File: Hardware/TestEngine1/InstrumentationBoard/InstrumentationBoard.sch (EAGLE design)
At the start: 109 parts, among them IC1 MAX31855, J1 1X2-3.5MM, Q1 MOSFET-NCHANNELBSS123LT1G, Q2 MOSFET-NCHANNELBSS123LT1G, Q3 MOSFET-NCHANNELBSS123LT1G, U1 BMP180

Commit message: work in progress in laying out and routing instrument board
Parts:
- removed C11: 0.33uF, SparkFun-Capacitors:CAP0805
- removed C12: 0.1uF, SparkFun-Capacitors:CAP0805
- removed D1: 1n4148, adafruit:DIODESOD-323F
- removed D2: 1N4148, adafruit:DIODESOD-323F
- removed JP20: (no value), SparkFun-Connectors:M03PTH
- removed JP21, JP22, JP23, JP24: M02PTH, SparkFun-Connectors:M02PTH
- removed R18: 10K, adafruit:R-US_R0805
- removed U$8: MC33269DTRK, RitLaunchInitiative:MC33269DTRK
- added JP133: (no value), SparkFun-Connectors:M05PTH
- added JP1777: M02PTH, SparkFun-Connectors:M02PTH
- added JP55: (no value), SparkFun-Connectors:M04PTH
- added R35: 10K, SparkFun-Resistors:RESISTOR0805-RES
- added U$10: BOOSTER_PACK_CONNECTED, RitLaunchInitiative:BOOSTER_PACK_CONNECTED
- C1, C2: device adafruit:C-USC0805K -> SparkFun-Capacitors:CAP0805
- JP11, JP14, JP15: value (none) -> M02PTH; device SparkFun-Connectors:M03PTH -> SparkFun-Connectors:M02PTH
- JP12, JP5: value (none) -> M02PTH; device SparkFun-Connectors:M04PTH -> SparkFun-Connectors:M02PTH
- JP13: value (none) -> M02PTH; device SparkFun-Connectors:M05PTH -> SparkFun-Connectors:M02PTH
- JP17, JP18, JP9: value M02PTH -> (none); device SparkFun-Connectors:M02PTH -> SparkFun-Connectors:M03PTH
- R1, R2, R8: value 10K -> 10k; device adafruit:R-US_R0805 -> SparkFun-Resistors:RESISTOR0805-RES
- R10, R11, R30, R34, R9: device adafruit:R-US_R0805 -> SparkFun-Resistors:RESISTOR0805-RES
- R12, R25: value 1.7k -> 10K
- R13, R26: value 3.3k -> 10K
- R14: value 68 -> 1.7k; device adafruit:R-US_R0805 -> SparkFun-Resistors:RESISTOR0805-RES
- R15: value 0 -> 3.3k; device adafruit:R-US_R0805 -> SparkFun-Resistors:RESISTOR0805-RES
- R16: value 0 -> 1.7k; device adafruit:R-US_R0805 -> SparkFun-Resistors:RESISTOR0805-RES
- R17: value 10K -> 3.3k; device adafruit:R-US_R0805 -> SparkFun-Resistors:RESISTOR0805-RES
- R19: value 10K -> 9k; device adafruit:R-US_R0805 -> SparkFun-Resistors:RESISTOR0805-RES
- R20: value 10K -> 3k; device adafruit:R-US_R0805 -> SparkFun-Resistors:RESISTOR0805-RES
- R21: value 10K -> 100; device adafruit:R-US_R0805 -> SparkFun-Resistors:RESISTOR0805-RES
- R22: value 9k -> 220; device adafruit:R-US_R0805 -> SparkFun-Resistors:RESISTOR0805-RES
- R23: value 3k -> 680; device adafruit:R-US_R0805 -> SparkFun-Resistors:RESISTOR0805-RES
- R24, R31, R32: value 10k -> 10K
- R27: value 100 -> 68; device adafruit:R-US_R0805 -> SparkFun-Resistors:RESISTOR0805-RES
- R28: value 220 -> 0; device adafruit:R-US_R0805 -> SparkFun-Resistors:RESISTOR0805-RES
- R29: value 680 -> 0; device adafruit:R-US_R0805 -> SparkFun-Resistors:RESISTOR0805-RES
- R33: value 10k -> 1K
- R7: value 1K -> 10k; device adafruit:R-US_R0805 -> SparkFun-Resistors:RESISTOR0805-RES
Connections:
- removed net SCLK: D1.C
- removed net THERMOCOUPLE_CS: D2.C
- new net KEYSWITCH_1: JP25.1, R31.1
- net +3V3: now also JP1777.2, JP5.2, JP6.2, JP7.2, JP8.2, R21.1, R28.1, R29.1, R34.1, R35.1, U$10.3.3V; no longer JP12.2, JP17.2, JP18.2, JP22.2, JP23.2, JP24.2, R1.1, R14.1, R15.1, R16.1, R2.1
- net 12V: now also JP11.2, JP12.2, JP13.2, JP133.5, JP14.2, JP15.2, R19.1, R23.1; no longer C11.1, JP12.4, JP13.5, JP21.2, JP6.2, JP7.2, JP8.2, JP9.2, R22.1, R29.1, U$8.IN
- net 5V: now also JP17.2, JP18.2, JP19.2, JP9.1, R22.1, U$10.5V; no longer C12.1, JP12.3, JP14.2, JP15.2, JP19.1, JP20.2, R28.1, U$8.OUT
- net BATTVOLTAGE: now also R19.2, R20.1, U$10.AIN19/PK3; no longer R22.2, R23.1
- net BLUE: now also R26.1; no longer R17.1
- net CS: now also R35.2; no longer D2.A, R2.2
- net FET1: now also R9.1, U$10.T0CCP1/PL5; no longer R8.1
- net FET2: now also R10.1, U$10.PL0; no longer R9.1
- net FET3: now also R11.1, U$10.PL1; no longer R10.1
- net FET4: now also R12.1, U$10.PL2; no longer R11.1
- net FET5: now also R13.1, U$10.PL3; no longer R30.1
- net GND: now also JP133.3, JP133.4, JP17.3, JP18.3, JP55.4, JP9.3, R1.1, R12.2, R13.2, R15.1, R17.1, R2.1, R24.2, R25.2, R26.2, R31.2, R32.2, R7.1, R8.1, U$10.GND; no longer JP11.1, JP12.1, JP13.3, JP13.4, JP14.3, JP15.3, JP20.3, JP5.4, R13.1, R17.2, R18.2, R19.2, R21.2, R23.2, R24.1, R26.1, R31.1, R32.1, R33.1, R34.2, R8.2
- net GREEN: now also R25.1; no longer R18.1
- net LOADCELL: now also U$10.AIN18/PK2
- net N$10: now also R28.2; no longer R15.2
- net N$11: now also JP55.1; no longer JP5.1
- net N$12: no longer C11.2, C12.2, U$8.GND
- net N$13: now also R33.2; no longer R7.2
- net N$14: now also R33.1; no longer R7.1
- net N$15: now also R29.2; no longer R16.2
- net N$16: now also JP55.2; no longer JP5.2
- net N$17: now also JP14.1; no longer JP9.1
- net N$18: now also JP11.1; no longer JP6.1
- net N$19: now also JP12.1; no longer JP7.1
- net N$2: now also JP9.2, R14.2; no longer JP10.2, R12.2
- net N$20: now also JP55.3; no longer JP5.3
- net N$21: now also JP10.2, R16.2; no longer JP19.2, R25.2
- net N$22: now also JP13.1; no longer JP8.1
- net N$23: now also R22.2; no longer R28.2
- net N$24: now also R21.2; no longer R27.2
- net N$25: now also R23.2; no longer R29.2
- net N$26: now also JP15.1; no longer JP21.1
- net N$9: now also R27.2; no longer R14.2
- net PSI_1: now also R14.1, R15.2, U$10.AIN16/PK0; no longer R12.1, R13.2
- net PSI_2: now also R16.1, R17.2, U$10.AIN17/PK1; no longer R25.1, R26.2
- net PWM_1: now also JP16.1, U$10.M0PWM1/PF1; no longer JP14.1
- net PWM_2: now also JP17.1, U$10.M0PWM2/PF2; no longer JP15.1
- net PWM_3: now also JP18.1, U$10.M0PWM3/PF3; no longer JP16.1
- net PWM_4: now also JP19.1, U$10.M0PWM4/PG0; no longer JP20.1
- net RED: now also R24.1; no longer R19.1
- net SCK: now also R34.2; no longer D1.A, R1.2
- net SCL: now also JP133.2, U$10.I2C0SCL/PB2; no longer JP11.2, JP13.2
- net SDA: now also JP133.1, U$10.I2C0SDA/PB3; no longer JP11.3, JP13.1
- net SW_1: now also R32.1; no longer R20.1
- net TILTSWITCH_1: now also JP1777.1, R30.1; no longer JP17.1, JP25.1, R21.1, R34.1
- net TR1: now also R1.2; no longer R3.2
- net TR2: now also R2.2; no longer R4.2
- net TR3: now also R3.2; no longer R5.2
- net TR4: now also R4.2; no longer R6.2
- net TR5: now also JP5.1, R5.2; no longer JP18.1, R24.2
- net TR6: now also JP6.1, R6.2, U$10.AIN13/PD2; no longer JP22.1, R31.2
- net TR7: now also JP7.1, R7.2, U$10.AIN10/PB4; no longer JP23.1, R32.2
- net TR8: now also JP8.1, R8.2, U$10.AIN11/PB5; no longer JP24.1, R33.2
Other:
- note removed: "I2c"
- note removed: "Optional for additional current sink"
- moved on the sheet: JP10, JP16, JP19, JP6, JP7, JP8, R1, R10, R11, R12, R13, R14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

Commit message: work in progress on pcb's
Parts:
- added JP20: (no value), SparkFun-Connectors:M03PTH
- added R18: 1.7k, SparkFun-Resistors:RESISTOR0805-RES
- added R36: 3.3k, SparkFun-Resistors:RESISTOR0805-RES
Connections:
- new net N$27: JP20.2, R18.2
- new net PSI_3: R18.1, R36.2, U$10.AIN18/PK2
- net 5V: now also JP20.1
- net BATTVOLTAGE: now also U$10.PA6; no longer U$10.AIN19/PK3
- net BLUE: now also U$10.M0PWM7/PK5
- net CS: now also U$10.PQ1
- net GND: now also JP20.3, R36.1
- net GREEN: now also U$10.M0PWM6/PK4
- net KEYSWITCH_1: now also U$10.PH1
- net LOADCELL: now also U$10.AIN19/PK3; no longer U$10.AIN18/PK2
- net MISO: now also U$10.SSI3RX/PQ3
- net RED: now also U$10.M0PWM5/PG1
- net SCK: now also U$10.SSI3CLK/PQ0
- net SW_1: now also U$10.PK6
- net TILTSWITCH_1: now also U$10.PH0
- net TR1: now also U$10.AIN3/PE0
- net TR2: now also U$10.AIN2/PE1
- net TR3: now also U$10.AIN1/PE2
- net TR4: now also U$10.AIN0/PE3
- net TR5: now also U$10.AIN4/PD7

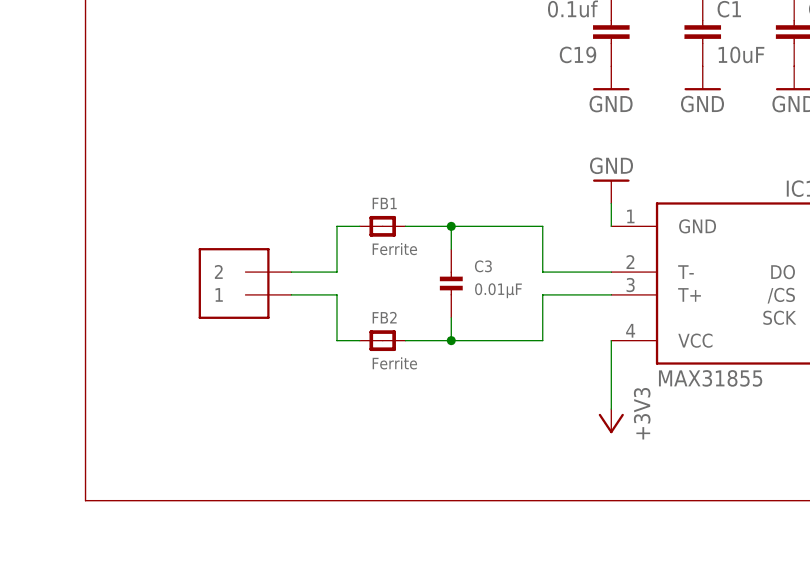
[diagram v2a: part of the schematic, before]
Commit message: power traces being layed out
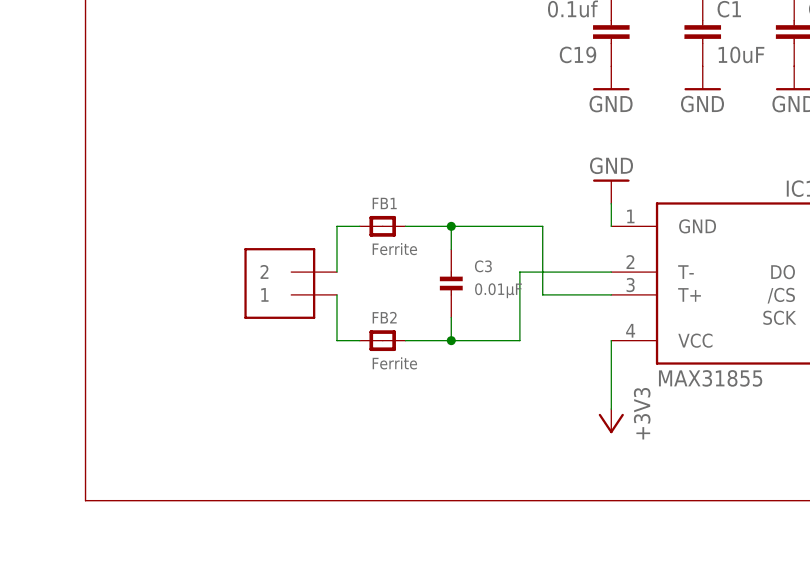
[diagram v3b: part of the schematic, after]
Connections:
- net N$4: now also IC1.T+; no longer IC1.T-
- net N$6: now also IC1.T-; no longer IC1.T+
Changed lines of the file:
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@@
 <instance part="IC1" gate="G$1" x="-88.9" y="134.62"/>
 <instance part="GND1" gate="1" x="-101.6" y="142.24" rot="R180"/>
-<instance part="J1" gate="G$1" x="-142.24" y="132.08" rot="R180"/>
+<instance part="J1" gate="G$1" x="-137.16" y="132.08" rot="R180"/>
 <instance part="+3V2" gate="G$1" x="-40.64" y="7.62"/>
 <instance part="+3V3" gate="G$1" x="-101.6" y="114.3" rot="R180"/>
@@
 <net name="N$1" class="0">
 <segment>
-<pinref part="J1" gate="G$1" pin="2"/>
-<wire x1="-137.16" y1="132.08" x2="-132.08" y2="132.08" width="0.1524" layer="91"/>
 <wire x1="-132.08" y1="132.08" x2="-132.08" y2="137.16" width="0.1524" layer="91"/>
 <pinref part="FB1" gate="G$1" pin="P$1"/>
 <wire x1="-132.08" y1="137.16" x2="-129.54" y2="137.16" width="0.1524" layer="91"/>
+<pinref part="J1" gate="G$1" pin="2"/>
 </segment>
 </net>
@@
 <wire x1="-119.38" y1="137.16" x2="-119.38" y2="134.62" width="0.1524" layer="91"/>
 <wire x1="-119.38" y1="137.16" x2="-109.22" y2="137.16" width="0.1524" layer="91"/>
-<wire x1="-109.22" y1="137.16" x2="-109.22" y2="132.08" width="0.1524" layer="91"/>
-<pinref part="IC1" gate="G$1" pin="T-"/>
-<wire x1="-109.22" y1="132.08" x2="-101.6" y2="132.08" width="0.1524" layer="91"/>
+<wire x1="-109.22" y1="137.16" x2="-109.22" y2="129.54" width="0.1524" layer="91"/>
 <junction x="-119.38" y="137.16"/>
+<pinref part="IC1" gate="G$1" pin="T+"/>
+<wire x1="-109.22" y1="129.54" x2="-101.6" y2="129.54" width="0.1524" layer="91"/>
 </segment>
 </net>
 <net name="N$5" class="0">
 <segment>
-<pinref part="J1" gate="G$1" pin="1"/>
-<wire x1="-137.16" y1="129.54" x2="-132.08" y2="129.54" width="0.1524" layer="91"/>
 <wire x1="-132.08" y1="129.54" x2="-132.08" y2="124.46" width="0.1524" layer="91"/>
 <pinref part="FB2" gate="G$1" pin="P$1"/>
 <wire x1="-132.08" y1="124.46" x2="-129.54" y2="124.46" width="0.1524" layer="91"/>
+<pinref part="J1" gate="G$1" pin="1"/>
 </segment>
 </net>
@@
 <wire x1="-124.46" y1="124.46" x2="-119.38" y2="124.46" width="0.1524" layer="91"/>
 <wire x1="-119.38" y1="124.46" x2="-119.38" y2="127" width="0.1524" layer="91"/>
-<wire x1="-119.38" y1="124.46" x2="-109.22" y2="124.46" width="0.1524" layer="91"/>
-<wire x1="-109.22" y1="124.46" x2="-109.22" y2="129.54" width="0.1524" layer="91"/>
+<wire x1="-119.38" y1="124.46" x2="-111.76" y2="124.46" width="0.1524" layer="91"/>
 <junction x="-119.38" y="124.46"/>
-<pinref part="IC1" gate="G$1" pin="T+"/>
-<wire x1="-109.22" y1="129.54" x2="-101.6" y2="129.54" width="0.1524" layer="91"/>
+<wire x1="-111.76" y1="124.46" x2="-111.76" y2="132.08" width="0.1524" layer="91"/>
+<pinref part="IC1" gate="G$1" pin="T-"/>
+<wire x1="-111.76" y1="132.08" x2="-101.6" y2="132.08" width="0.1524" layer="91"/>
 </segment>
 </net>

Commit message: majority of power and analog busses layed out
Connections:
- net BATTVOLTAGE: now also U$10.AIN19/PK3; no longer U$10.PA6
- net FET2: now also U$10.PL3; no longer U$10.PL0
- net FET3: now also U$10.PL0; no longer U$10.PL1
- net FET4: now also U$10.PL1; no longer U$10.PL2
- net FET5: now also U$10.PL2; no longer U$10.PL3
- net GND: now also JP10.2, JP20.2, JP9.2; no longer JP10.3, JP20.3, JP9.3
- net LOADCELL: now also U$10.AIN13/PD2; no longer U$10.AIN19/PK3
- net N$2: now also JP9.3; no longer JP9.2
- net N$21: now also JP10.3; no longer JP10.2
- net N$27: now also JP20.3; no longer JP20.2
- net PSI_1: now also U$10.AIN11/PB5; no longer U$10.AIN16/PK0
- net PSI_2: now also U$10.AIN16/PK0; no longer U$10.AIN17/PK1
- net PSI_3: now also U$10.AIN10/PB4; no longer U$10.AIN18/PK2
- net TR6: now also U$10.PA6; no longer U$10.AIN13/PD2
- net TR7: now also U$10.AIN17/PK1; no longer U$10.AIN10/PB4
- net TR8: now also U$10.AIN18/PK2; no longer U$10.AIN11/PB5
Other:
- moved on the sheet: JP10, JP9, R18

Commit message: work in progress
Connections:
- net GREEN: now also U$10.M0PWM5/PG1; no longer U$10.M0PWM6/PK4
- net RED: now also U$10.M0PWM6/PK4; no longer U$10.M0PWM5/PG1
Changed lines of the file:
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@@
 <segment>
 <wire x1="-50.8" y1="213.36" x2="-66.04" y2="213.36" width="0.1524" layer="91"/>
+<pinref part="U$10" gate="G$1" pin="M0PWM7/PK5"/>
 <label x="-50.8" y="213.36" size="1.016" layer="95" xref="yes"/>
-<pinref part="U$10" gate="G$1" pin="M0PWM7/PK5"/>
 </segment>
 </net>
@@
 </segment>
 <segment>
-<wire x1="-50.8" y1="215.9" x2="-66.04" y2="215.9" width="0.1524" layer="91"/>
-<label x="-50.8" y="215.9" size="1.016" layer="95" xref="yes"/>
-<pinref part="U$10" gate="G$1" pin="M0PWM6/PK4"/>
+<wire x1="-48.26" y1="218.44" x2="-66.04" y2="218.44" width="0.1524" layer="91"/>
+<label x="-48.26" y="218.44" size="1.016" layer="95" xref="yes"/>
+<pinref part="U$10" gate="G$1" pin="M0PWM5/PG1"/>
 </segment>
 </net>
@@
 </segment>
 <segment>
-<wire x1="-50.8" y1="218.44" x2="-66.04" y2="218.44" width="0.1524" layer="91"/>
-<label x="-50.8" y="218.44" size="1.016" layer="95" xref="yes"/>
-<pinref part="U$10" gate="G$1" pin="M0PWM5/PG1"/>
+<wire x1="-66.04" y1="215.9" x2="-55.88" y2="215.9" width="0.1524" layer="91"/>
+<label x="-55.88" y="215.9" size="1.016" layer="95" xref="yes"/>
+<pinref part="U$10" gate="G$1" pin="M0PWM6/PK4"/>
 </segment>
 </net>

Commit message: more work on board
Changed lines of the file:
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@@
 <wire x1="325.12" y1="220.98" x2="325.12" y2="289.56" width="0.1524" layer="94"/>
 <wire x1="325.12" y1="289.56" x2="190.5" y2="289.56" width="0.1524" layer="94"/>
-<text x="218.44" y="287.02" size="2.54" layer="94">Pressure transducers voltage signaling</text>
+<text x="226.06" y="284.48" size="2.54" layer="94">Pressure transducers voltage signaling</text>
 <wire x1="195.58" y1="106.68" x2="325.12" y2="106.68" width="0.1524" layer="94"/>
 <wire x1="325.12" y1="106.68" x2="325.12" y2="71.12" width="0.1524" layer="94"/>

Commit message: Finished bulk routing.
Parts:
- removed C16: 10uF, SparkFun-Capacitors:CAP0805
- removed C17: 0.1uf, SparkFun-Capacitors:CAP0805
- removed C18: 100pF, SparkFun-Capacitors:CAP0805
- added R37, R38: 10K, SparkFun-Resistors:RESISTOR0805-RES
- added S2: SWITCH-MOMENTARY-2SMD, SparkFun-Electromechanical:SWITCH-MOMENTARY-2SMD
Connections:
- new net RST: S2.1, U$10.RST
- net +3V3: now also R37.1, R38.1
- net 12V: no longer C16.1, C17.1, C18.1
- net GND: now also S2.2; no longer C16.2, C17.2, C18.2
- net SCL: now also R37.2
- net SDA: now also R38.2
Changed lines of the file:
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@@
 <part name="SUPPLY22" library="SparkFun-Aesthetics" deviceset="12V" device=""/>
 <part name="SUPPLY23" library="SparkFun-Aesthetics" deviceset="12V" device=""/>
-<part name="C16" library="SparkFun-Capacitors" deviceset="CAP" device="0805" value="10uF">
-<attribute name="DIGIKEY" value="490-3886-1-ND"/>
-</part>
-<part name="C17" library="SparkFun-Capacitors" deviceset="CAP" device="0805" value="0.1uf"/>
-<part name="C18" library="SparkFun-Capacitors" deviceset="CAP" device="0805" value="100pF"/>
 <part name="SUPPLY24" library="SparkFun-Aesthetics" deviceset="12V" device=""/>
 <part name="GND47" library="supply1" deviceset="GND" device=""/>
@@
 <part name="R36" library="SparkFun-Resistors" deviceset="RESISTOR" device="0805-RES" value="3.3k"/>
 <part name="GND29" library="supply1" deviceset="GND" device=""/>
+<part name="R37" library="SparkFun-Resistors" deviceset="RESISTOR" device="0805-RES" value="10K"/>
+<part name="R38" library="SparkFun-Resistors" deviceset="RESISTOR" device="0805-RES" value="10K"/>
+<part name="+3V23" library="supply1" deviceset="+3V3" device=""/>
+<part name="+3V24" library="supply1" deviceset="+3V3" device=""/>
+<part name="S2" library="SparkFun-Electromechanical" deviceset="SWITCH-MOMENTARY-2" device="SMD"/>
+<part name="GND60" library="supply1" deviceset="GND" device=""/>
 </parts>
 <sheets>
@@
 <instance part="SUPPLY22" gate="G$1" x="-165.1" y="-40.64"/>
 <instance part="SUPPLY23" gate="G$1" x="-157.48" y="-40.64"/>
-<instance part="C16" gate="G$1" x="-157.48" y="-66.04">
-<attribute name="DIGIKEY" x="-157.48" y="-66.04" size="1.016" layer="96" display="off"/>
-</instance>
-<instance part="C17" gate="G$1" x="-165.1" y="-66.04"/>
-<instance part="C18" gate="G$1" x="-172.72" y="-66.04"/>
 <instance part="SUPPLY24" gate="G$1" x="-172.72" y="-60.96"/>
 <instance part="GND47" gate="1" x="-172.72" y="-71.12"/>
 <instance part="GND48" gate="1" x="-165.1" y="-71.12"/>
-<instance part="GND49" gate="1" x="-157.48" y="-71.12"/>
+<instance part="GND49" gate="1" x="-154.94" y="-71.12"/>
 <instance part="SUPPLY25" gate="G$1" x="-165.1" y="-60.96"/>
-<instance part="SUPPLY26" gate="G$1" x="-157.48" y="-60.96"/>
+<instance part="SUPPLY26" gate="G$1" x="-154.94" y="-60.96"/>
 <instance part="C19" gate="G$1" x="-101.6" y="160.02" rot="R180"/>
 <instance part="+3V17" gate="G$1" x="-101.6" y="167.64"/>
@@
 <instance part="R36" gate="G$1" x="302.26" y="238.76" rot="MR90"/>
 <instance part="GND29" gate="1" x="302.26" y="228.6" rot="MR0"/>
+<instance part="R37" gate="G$1" x="-180.34" y="297.18" rot="R270"/>
+<instance part="R38" gate="G$1" x="-172.72" y="299.72" rot="R270"/>
+<instance part="+3V23" gate="G$1" x="-180.34" y="309.88"/>
+<instance part="+3V24" gate="G$1" x="-172.72" y="309.88"/>
+<instance part="S2" gate="G$1" x="157.48" y="-63.5"/>
+<instance part="GND60" gate="1" x="165.1" y="-71.12"/>
 </instances>
 <busses>
@@
 </segment>
 <segment>
-<pinref part="C18" gate="G$1" pin="2"/>
-<pinref part="GND47" gate="1" pin="GND"/>
-</segment>
-<segment>
-<pinref part="C17" gate="G$1" pin="2"/>
-<pinref part="GND48" gate="1" pin="GND"/>
-</segment>
-<segment>
-<pinref part="C16" gate="G$1" pin="2"/>
-<pinref part="GND49" gate="1" pin="GND"/>
-</segment>
-<segment>
 <pinref part="C19" gate="G$1" pin="1"/>
 <pinref part="GND50" gate="1" pin="GND"/>
@@
 <pinref part="R36" gate="G$1" pin="1"/>
 <wire x1="302.26" y1="231.14" x2="302.26" y2="233.68" width="0.1524" layer="91"/>
+</segment>
+<segment>
+<pinref part="S2" gate="G$1" pin="2"/>
+<pinref part="GND60" gate="1" pin="GND"/>
+<wire x1="162.56" y1="-63.5" x2="165.1" y2="-63.5" width="0.1524" layer="91"/>
+<wire x1="165.1" y1="-63.5" x2="165.1" y2="-68.58" width="0.1524" layer="91"/>
 </segment>
 </net>
@@
 <wire x1="-121.92" y1="294.64" x2="-129.54" y2="294.64" width="0.1524" layer="91"/>
 <wire x1="-129.54" y1="294.64" x2="-129.54" y2="299.72" width="0.1524" layer="91"/>
+</segment>
+<segment>
+<pinref part="R37" gate="G$1" pin="1"/>
+<pinref part="+3V23" gate="G$1" pin="+3V3"/>
+<wire x1="-180.34" y1="307.34" x2="-180.34" y2="302.26" width="0.1524" layer="91"/>
+</segment>
+<segment>
+<pinref part="R38" gate="G$1" pin="1"/>
+<pinref part="+3V24" gate="G$1" pin="+3V3"/>
+<wire x1="-172.72" y1="307.34" x2="-172.72" y2="304.8" width="0.1524" layer="91"/>
 </segment>
 </net>
@@
 </segment>
 <segment>
-<pinref part="C18" gate="G$1" pin="1"/>
-<pinref part="SUPPLY24" gate="G$1" pin="12V"/>
-</segment>
-<segment>
-<pinref part="C17" gate="G$1" pin="1"/>
-<pinref part="SUPPLY25" gate="G$1" pin="12V"/>
-</segment>
-<segment>
-<pinref part="C16" gate="G$1" pin="1"/>
-<pinref part="SUPPLY26" gate="G$1" pin="12V"/>
-</segment>
-<segment>
 <pinref part="R23" gate="G$1" pin="1"/>
 <pinref part="SUPPLY28" gate="G$1" pin="12V"/>
@@
 <label x="-134.62" y="271.78" size="1.016" layer="95" rot="R180" xref="yes"/>
 </segment>
+<segment>
+<wire x1="-157.48" y1="287.02" x2="-172.72" y2="287.02" width="0.1524" layer="91"/>
+<pinref part="R38" gate="G$1" pin="2"/>
+<wire x1="-172.72" y1="287.02" x2="-172.72" y2="294.64" width="0.1524" layer="91"/>
+<label x="-157.48" y="287.02" size="1.016" layer="95" xref="yes"/>
+</segment>
 </net>
 <net name="SCL" class="0">
@@
 <pinref part="U$10" gate="G$1" pin="I2C0SCL/PB2"/>
 <label x="-134.62" y="274.32" size="1.016" layer="95" rot="R180" xref="yes"/>
+</segment>
+<segment>
+<wire x1="-157.48" y1="284.48" x2="-180.34" y2="284.48" width="0.1524" layer="91"/>
+<pinref part="R37" gate="G$1" pin="2"/>
+<wire x1="-180.34" y1="284.48" x2="-180.34" y2="292.1" width="0.1524" layer="91"/>
+<label x="-157.48" y="284.48" size="1.016" layer="95" xref="yes"/>
 </segment>
 </net>
@@
 </segment>
 </net>
+<net name="RST" class="0">
+<segment>
+<pinref part="U$10" gate="G$1" pin="RST"/>
+<wire x1="-66.04" y1="233.68" x2="-53.34" y2="233.68" width="0.1524" layer="91"/>
+<label x="-53.34" y="233.68" size="1.016" layer="95" xref="yes"/>
+</segment>
+<segment>
+<pinref part="S2" gate="G$1" pin="1"/>
+<wire x1="152.4" y1="-63.5" x2="144.78" y2="-63.5" width="0.1524" layer="91"/>
+<label x="144.78" y="-63.5" size="1.016" layer="95" rot="R180" xref="yes"/>
+</segment>
+</net>
